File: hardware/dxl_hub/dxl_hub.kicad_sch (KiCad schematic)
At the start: 12 parts, among them CN1 B3B-EH-A (LF)(SN), CN2 B3B-PH-K-S(LF)(SN), CN3 B3B-EH-A (LF)(SN), CN4 B3B-PH-K-S(LF)(SN), CN5 B3B-EH-A (LF)(SN), CN6 B3B-PH-K-S(LF)(SN), CN7 B3B-EH-A (LF)(SN), CN8 B3B-PH-K-S(LF)(SN), J1 1.8mm螺丝孔, J2 1.8mm螺丝孔

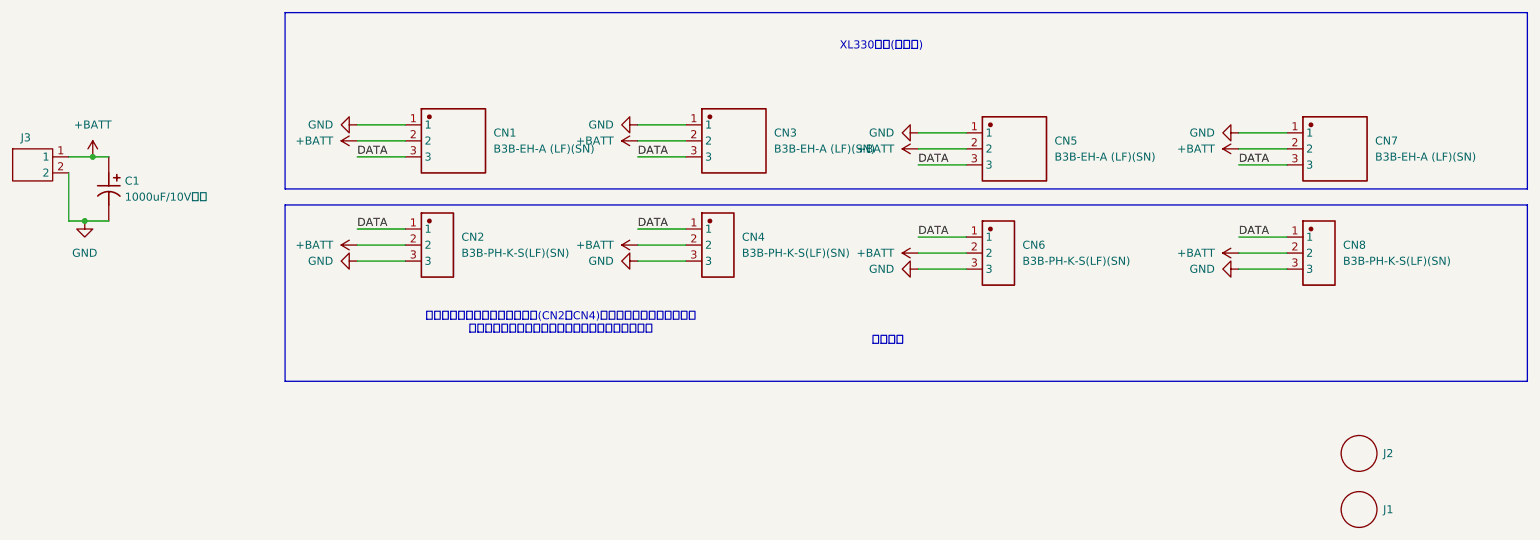
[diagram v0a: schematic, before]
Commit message: 更正原理图规格型号
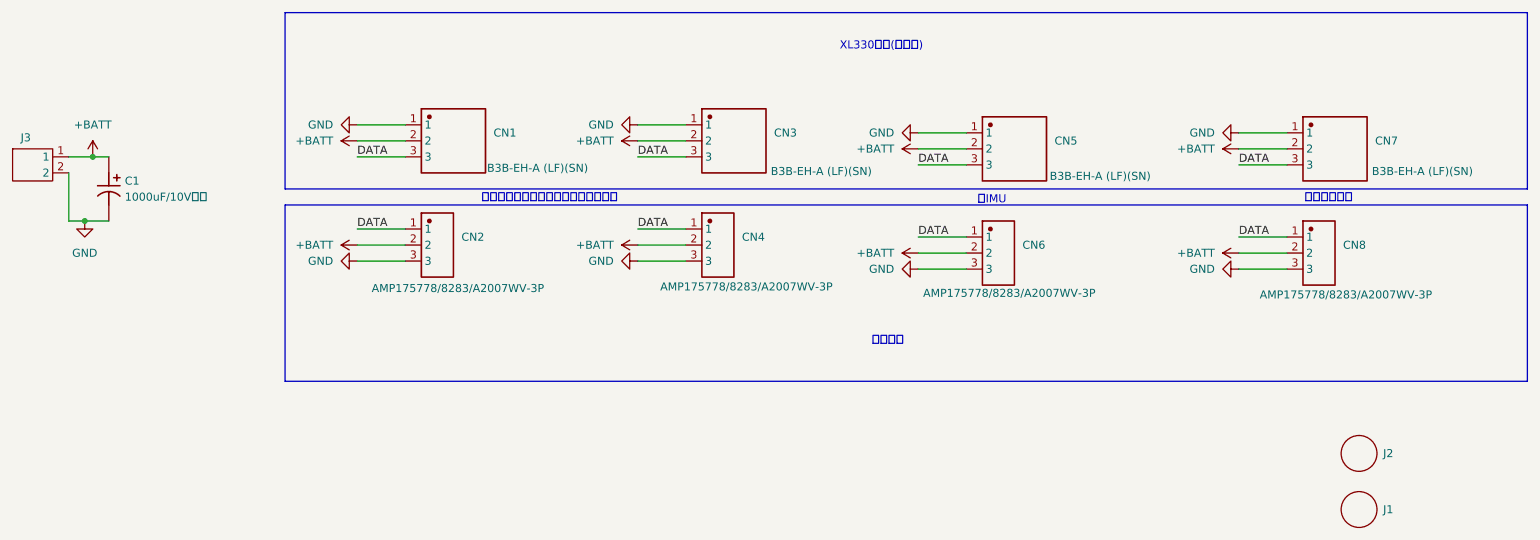
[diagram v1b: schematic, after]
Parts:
- CN2, CN4, CN6, CN8: value B3B-PH-K-S(LF)(SN) -> AMP175778/8283/A2007WV-3P
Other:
- note added: "接IMU"
- note added: "接颈部舵机线"
- note added: "正面左右腿舵机线束需要绕到背面插上"
- note removed: "上一版本发现正面焊接卧式插座(CN2、CN4)，与鸭脖子舵机有少许干涉 改为背面立式插座，正面舵机线束需要绕到背面插上"
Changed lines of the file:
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@@
+		)
+	)
+	(text "接颈部舵机线"
+		(exclude_from_sim no)
+		(at 246.634 78.994 0)
+		(effects
+			(font
+				(size 1.27 1.27)
+			)
+		)
+	)
+	(text "接IMU"
+		(exclude_from_sim no)
+		(at 193.294 79.248 0)
+		(effects
+			(font
+				(size 1.27 1.27)
+			)
 		)
 	)
@@
 		)
 	)
-	(text "上一版本发现正面焊接卧式插座(CN2、CN4)，与鸭脖子舵机有少许干涉\n改为背面立式插座，正面舵机线束需要绕到背面插上"
-		(exclude_from_sim no)
-		(at 124.968 98.806 0)
+	(text "正面左右腿舵机线束需要绕到背面插上"
+		(exclude_from_sim no)
+		(at 123.19 78.994 0)
 		(effects
 			(font
@@
 		(on_board yes)
 		(dnp no)
-		(fields_autoplaced yes)
 		(property "Reference" "CN4"
 			(at 153.67 85.0899 0)
@@
 			)
 		)
-		(property "Value" "B3B-PH-K-S(LF)(SN)"
-			(at 153.67 87.6299 0)
+		(property "Value" "AMP175778/8283/A2007WV-3P"
+			(at 140.716 92.964 0)
 			(effects
 				(font
@@
 		(on_board yes)
 		(dnp no)
-		(fields_autoplaced yes)
 		(property "Reference" "CN8"
 			(at 248.92 86.3599 0)
@@
 			)
 		)
-		(property "Value" "B3B-PH-K-S(LF)(SN)"
-			(at 248.92 88.8999 0)
+		(property "Value" "AMP175778/8283/A2007WV-3P"
+			(at 235.712 94.234 0)
 			(effects
 				(font
@@
 		(on_board yes)
 		(dnp no)
-		(fields_autoplaced yes)
 		(property "Reference" "CN1"
 			(at 114.3 68.5799 0)
@@
 		)
 		(property "Value" "B3B-EH-A (LF)(SN)"
-			(at 114.3 71.1199 0)
+			(at 113.284 74.168 0)
 			(effects
 				(font
@@
 		(on_board yes)
 		(dnp no)
-		(fields_autoplaced yes)
 		(property "Reference" "CN5"
 			(at 203.2 69.8499 0)
@@
 		)
 		(property "Value" "B3B-EH-A (LF)(SN)"
-			(at 203.2 72.3899 0)
+			(at 202.438 75.438 0)
 			(effects
 				(font
@@
 		(on_board yes)
 		(dnp no)
-		(fields_autoplaced yes)
 		(property "Reference" "CN3"
 			(at 158.75 68.5799 0)
@@
 		)
 		(property "Value" "B3B-EH-A (LF)(SN)"
-			(at 158.75 71.1199 0)
+			(at 158.242 74.676 0)
 			(effects
 				(font
@@
 		(on_board yes)
 		(dnp no)
-		(fields_autoplaced yes)
 		(property "Reference" "CN7"
 			(at 254 69.8499 0)
@@
 		)
 		(property "Value" "B3B-EH-A (LF)(SN)"
-			(at 254 72.3899 0)
+			(at 253.492 74.676 0)
 			(effects
 				(font
@@
 		(on_board yes)
 		(dnp no)
-		(fields_autoplaced yes)
 		(property "Reference" "CN2"
 			(at 109.22 85.0899 0)
@@
 			)
 		)
-		(property "Value" "B3B-PH-K-S(LF)(SN)"
-			(at 109.22 87.6299 0)
+		(property "Value" "AMP175778/8283/A2007WV-3P"
+			(at 94.996 93.218 0)
 			(effects
 				(font
@@
 		(on_board yes)
 		(dnp no)
-		(fields_autoplaced yes)
 		(property "Reference" "CN6"
 			(at 198.12 86.3599 0)
@@
 			)
 		)
-		(property "Value" "B3B-PH-K-S(LF)(SN)"
-			(at 198.12 88.8999 0)
-			(effects
-				(font
+		(property "Value" "AMP175778/8283/A2007WV-3P"
+			(at 182.372 93.98 0)
+			(effects
+				(font
